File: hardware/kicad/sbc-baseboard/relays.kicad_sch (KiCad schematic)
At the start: 30 parts, among them J11 Relay COM/NO/NC, J12 Relay COM/NO/NC, J18 PSU in (isolated), J19 PSU out (isolated), K801 G6K-2F-Y DC5, K802 G6K-2F-Y DC5, K803 JW1FSN-DC5V, Q801 2N7002, Q802 2N7002, Q803 AO3400A, U801 LTV-817

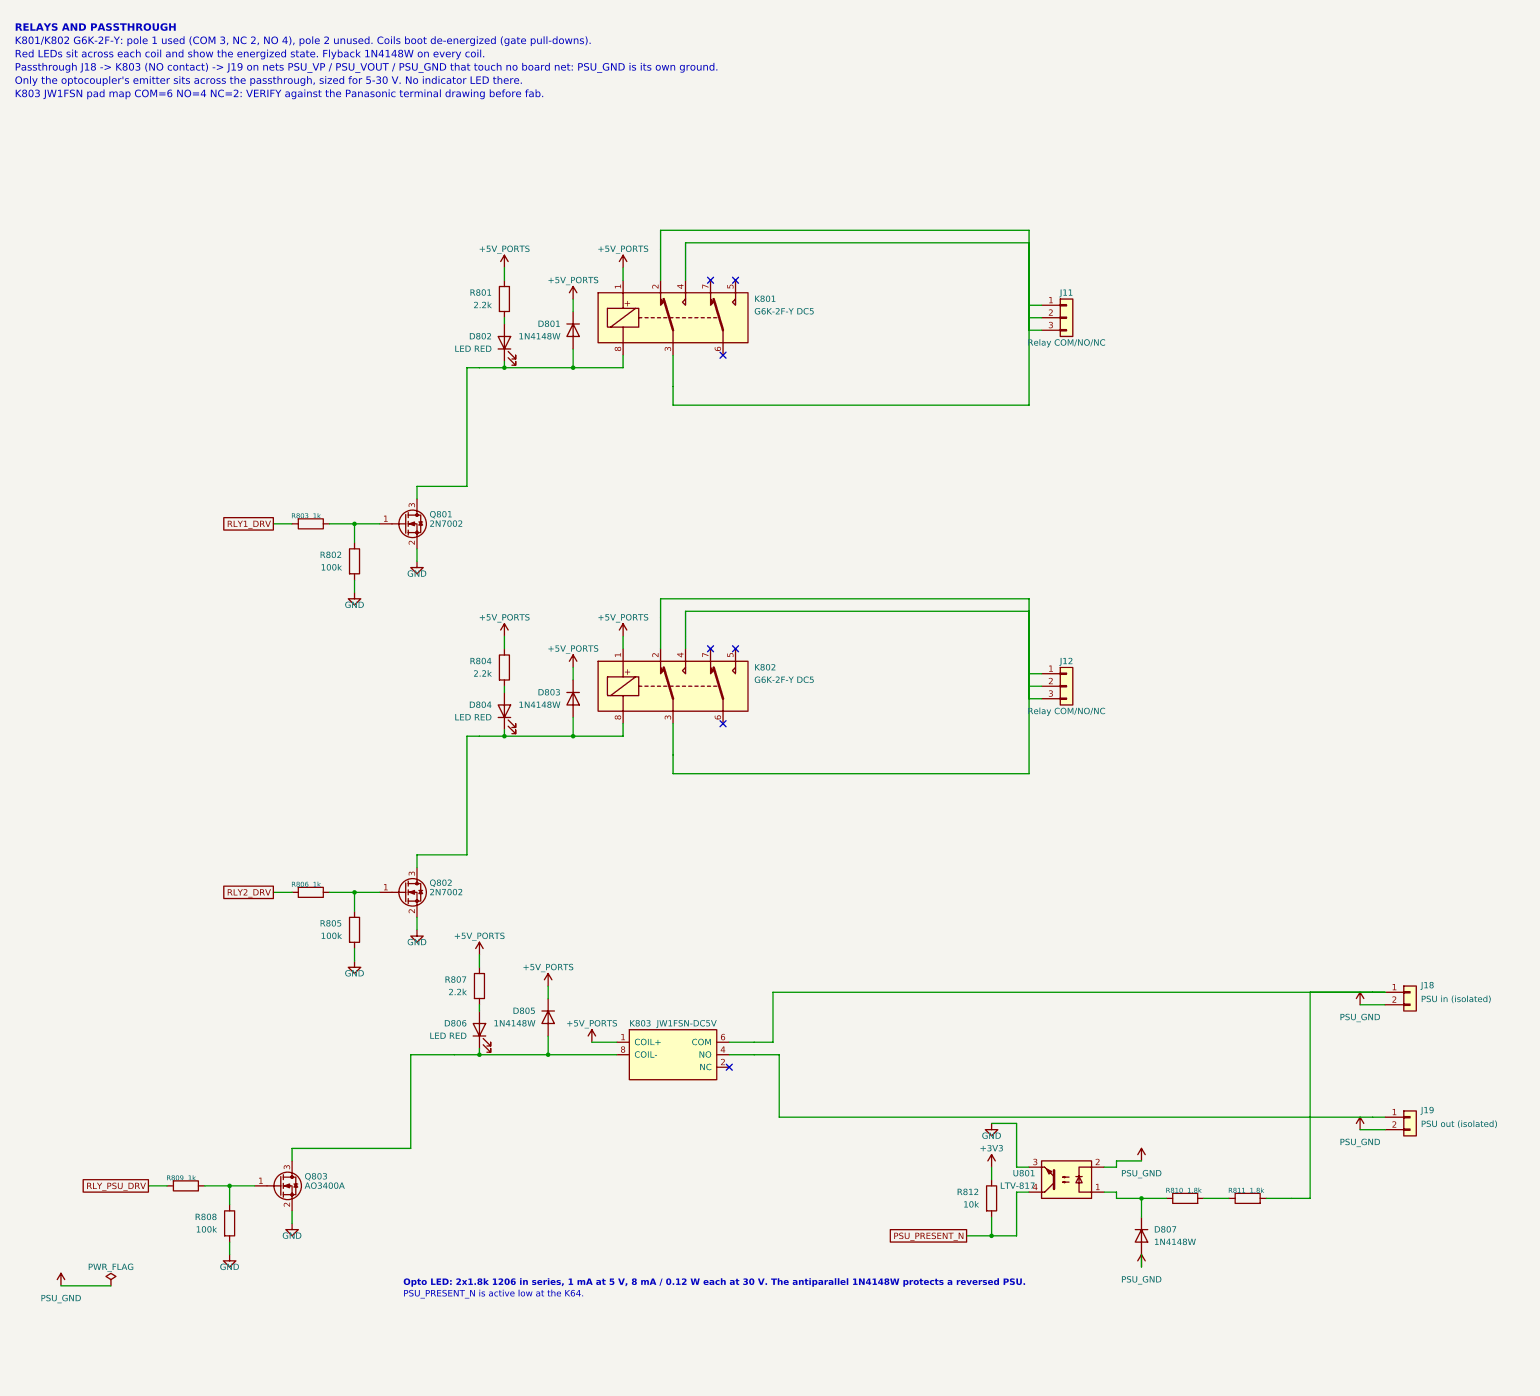
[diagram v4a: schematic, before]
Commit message: Reference-design review; pin numbers and real text widths in the layout gate
Review (docs/reference-design-review.md): every IC's surrounding parts
compared with its datasheet typical application or evaluation board.
Brought in line:
- TPS54560B compensation 16.9k / 4.7 nF / 47 pF (the 5 V / 400 kHz design
  example, same 141 uF ceramic output); the placeholders are gone.
- TPS62823 divider 453k / 100k with the 120 pF feed-forward capacitor the
  datasheet recommends.
- USB2517 VBUS_DET from the EVB: 100k / 100k with 1 uF (was 10k / 22k, 3.4 V
  at a 3.3 V pin).
- KSZ8081 MDIO pull-up 1.0k as the datasheet requires (was 4.7k).
- FT231X: 27 R in series and 47 pF on USBDM/USBDP, datasheet figure 6.1.
Deviations kept and documented: the bucks' EN gated by the PD controller
instead of a UVLO divider, the FT231X fed by a power switch instead of a
ferrite bead, translator OE tied to the target rail.

Layout gate: pin numbers are text boxes like any other, and all text widths
come from a per-glyph table fitted to the extents KiCad writes into its PDF
(check_pins.py); the generator's spacing uses the same table. That exposed
and fixed: reference/value overlaps on narrow symbols (now stacked), rail
names printed over each other (the lane end and hanging pull-up now carry
half the rail name), a port-switch value over its pin number, turned parts
with text on the pin side, lane stacks whose spread collapsed at the grid
snap, routes landing on connector pin stubs (J16, J601, J14, D202 moved),
the PD controller's I2C and gate routes that crossed half the sheet (now
labels), and the port /FAULT and I2C1 pull-ups, which as hanging resistors
staggered off the sheet and are now one column to one +3V3 symbol. The
port switch carries FAULT above OUT so the switched rail's parts hang below
the label; the VBUS row is drawn from the connector back to the switch.

All sheets: ERC 0, contacts 0, merges 0, layout 0 in every category.
Connectivity against 8579cd2 differs only in the value ch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
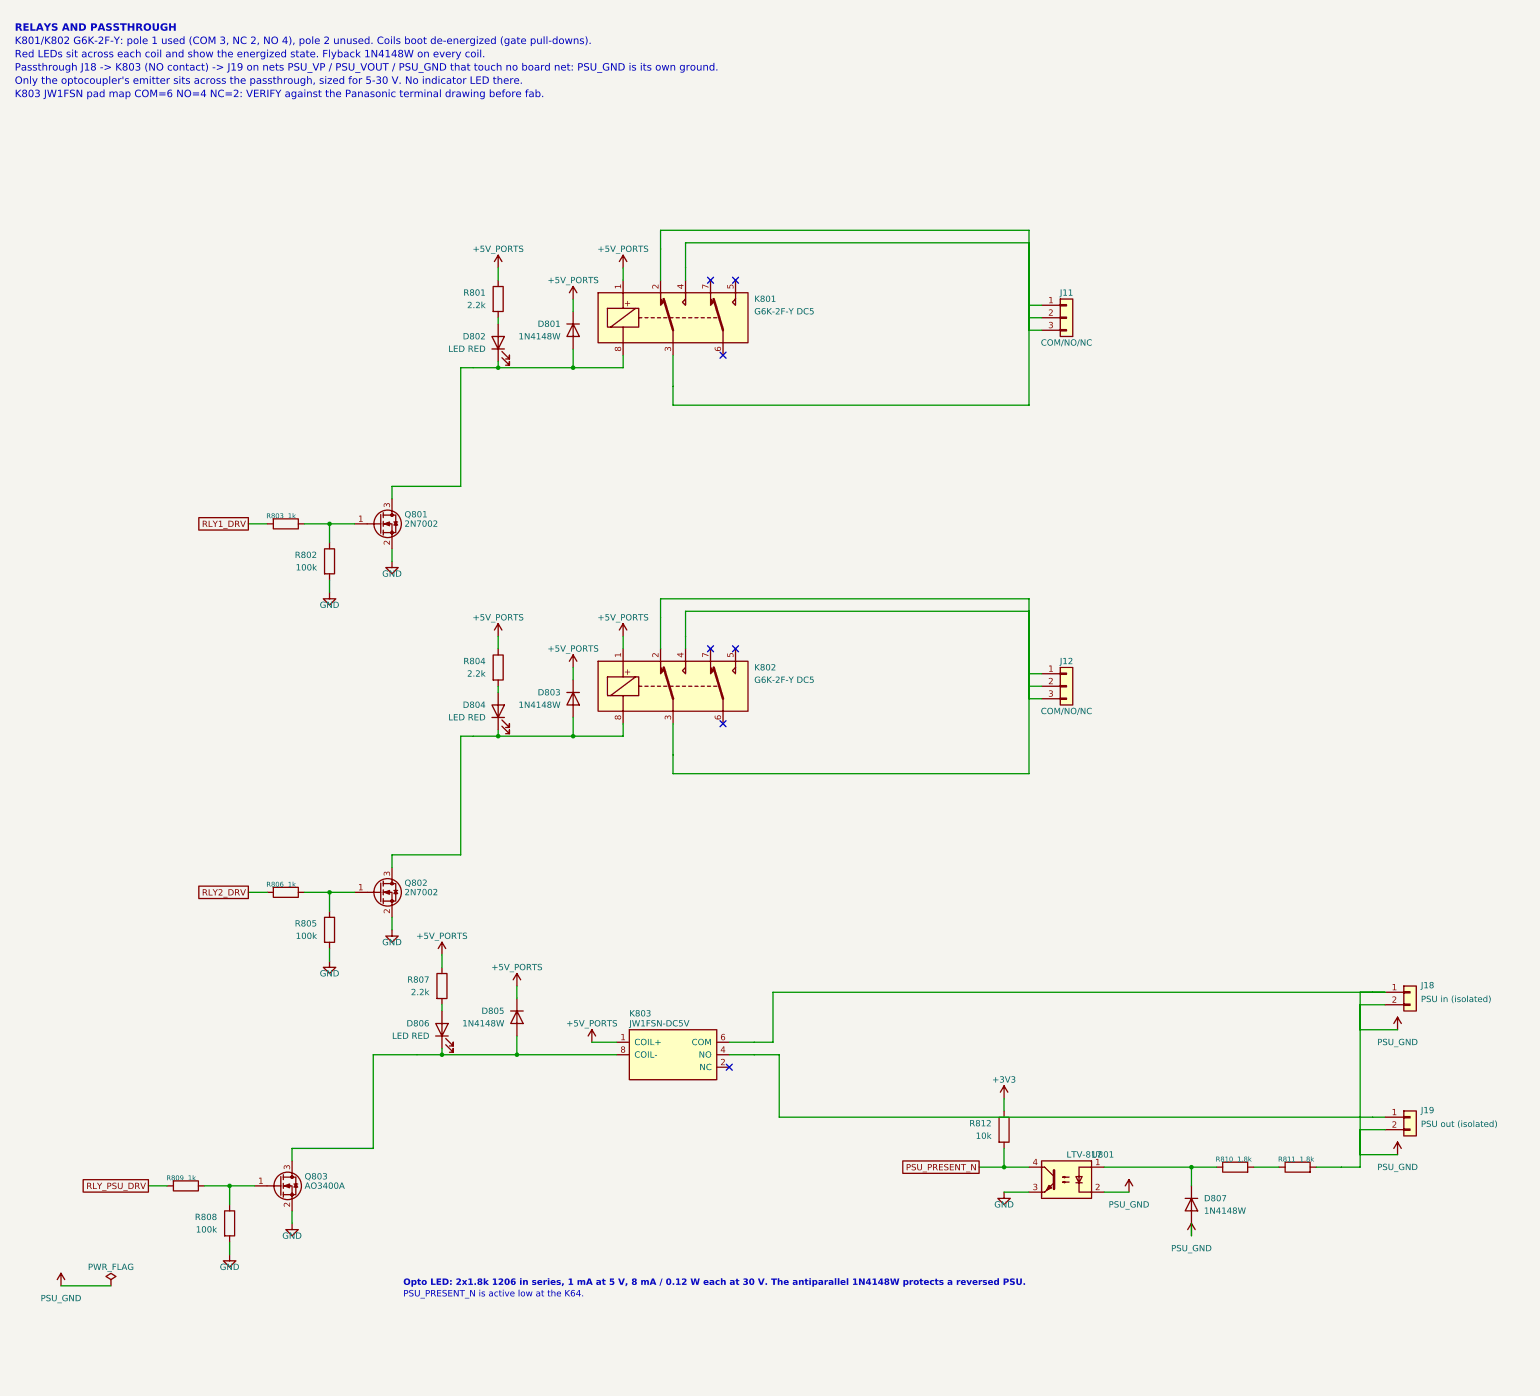
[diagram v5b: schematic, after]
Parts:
- J11, J12: value Relay COM/NO/NC -> COM/NO/NC
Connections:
- net PSU_GND: now also J18.1 (Pin_1), K803.6 (COM), R811.2

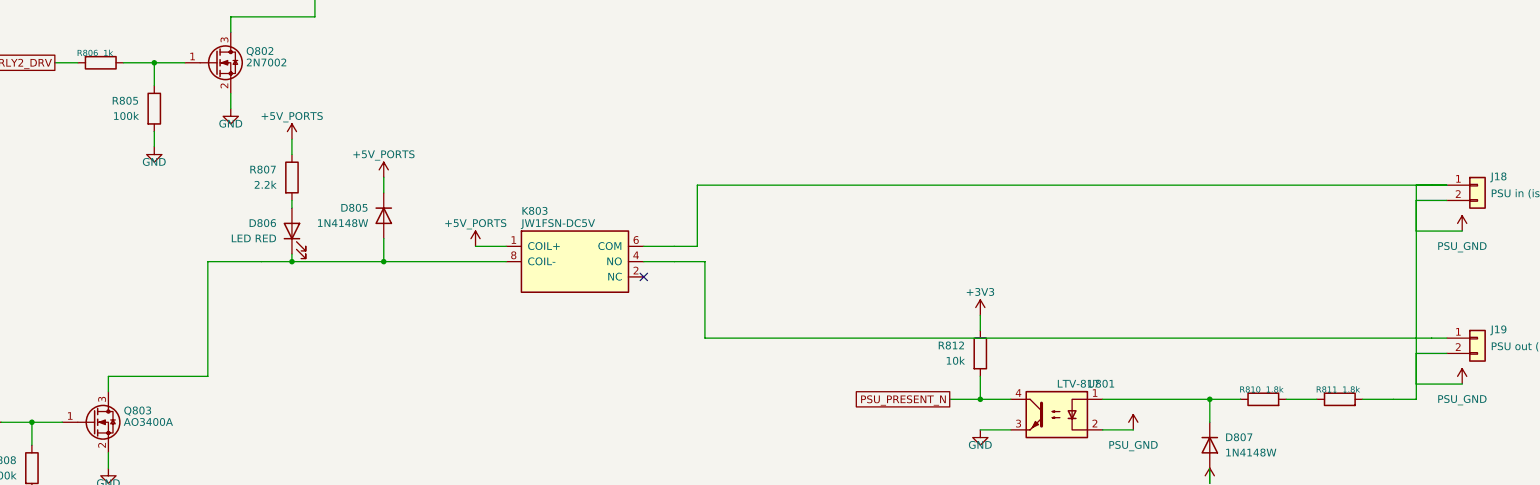
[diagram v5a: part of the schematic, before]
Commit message: House symbols from the ecad-libraries submodule
The project symbols move to calicopizzadelivery/ecad-libraries, added as a
submodule at hardware/kicad/libs and pinned to v0.1.1. The generator loads
them from the submodule's files (kisym.EXTRA_LIBS), so the embedded copies
match the library exactly; sym-lib-table and fp-lib-table are the fragments
the library ships, naming calico-ic and calico-electromechanical as
${KIPRJMOD}/../libs/... gen/parts.py and the project .kicad_sym are gone.

The symbols now follow the KiCad Library Conventions (every pin on the 100 mil
grid of the origin, 20 mil name offset), which moved a few pin rows; the port
blocks are re-aligned to the stacked USB-A's new rows. All sheets: ERC 0,
contacts 0, merges 0, layout 0; connectivity unchanged.

Co-Authored-By: Claude Fable 5.1 <noreply@anthropic.com>
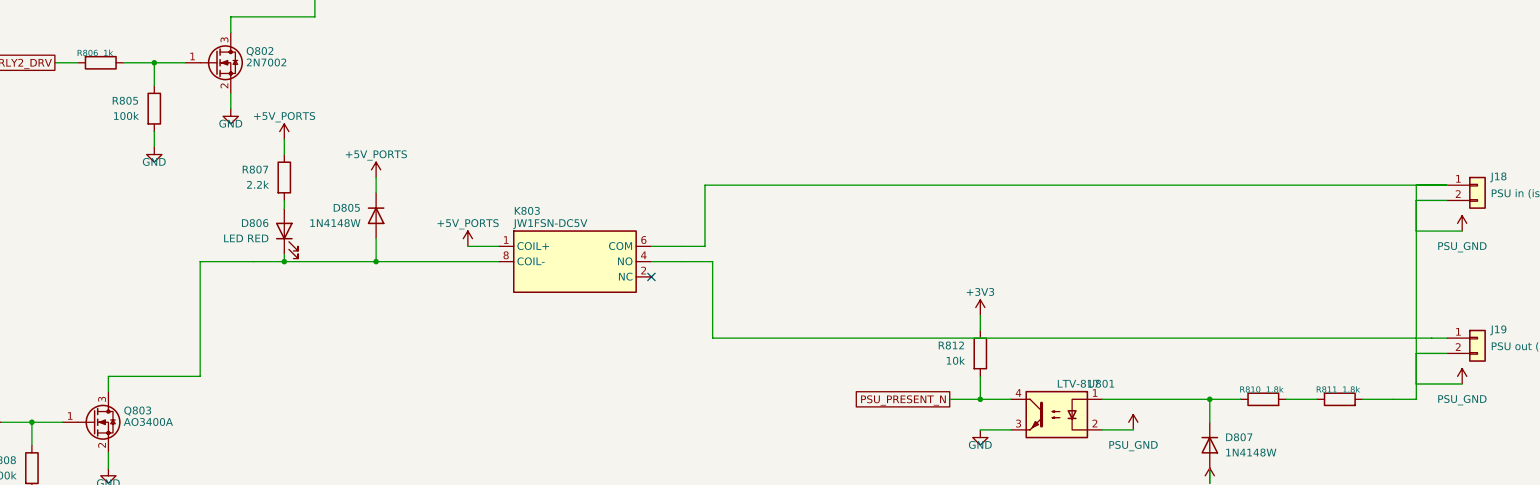
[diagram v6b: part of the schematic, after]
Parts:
- removed K803: JW1FSN-DC5V, Relay_THT:Relay_SPDT_Panasonic_JW1_FormC, symbol sbcbb:JW1FSN
- added K803: JW1FSN-DC5V, Relay_THT:Relay_SPDT_Panasonic_JW1_FormC, symbol calico-electromechanical:JW1FSN
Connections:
- net +5V_PORTS: now also K803.1 (COIL+)
- net PSU_GND: now also K803.6 (COM)
- net at J19.1 (Pin_1): now also K803.4 (NO)
- net at D805.2 (A), D806.1 (K), Q803.3 (D): now also K803.8 (COIL-)
